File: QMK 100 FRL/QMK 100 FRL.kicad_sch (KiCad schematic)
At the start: 16 parts

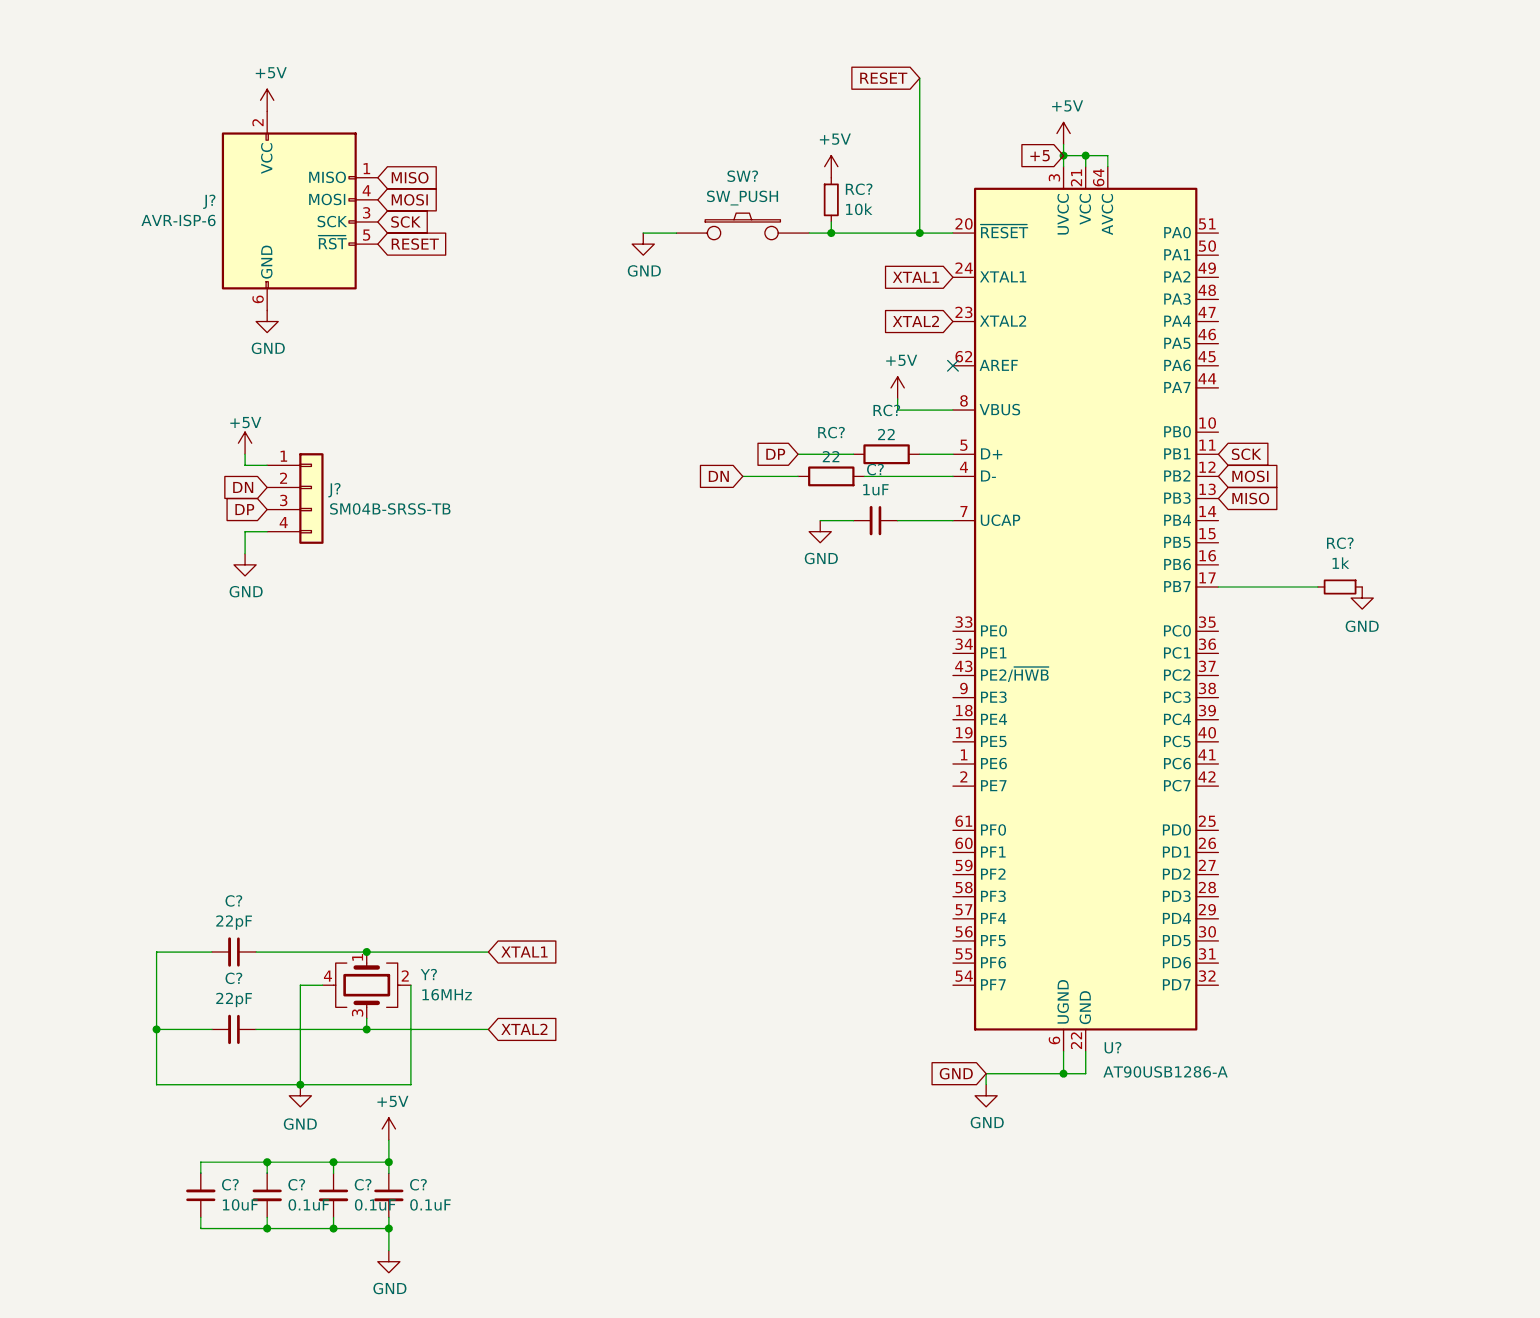
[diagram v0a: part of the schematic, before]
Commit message: Changed MCU
Changed MCU from ATMEL AT90USB1286-AUR to ATMEGA128A-AU which is the newest version.
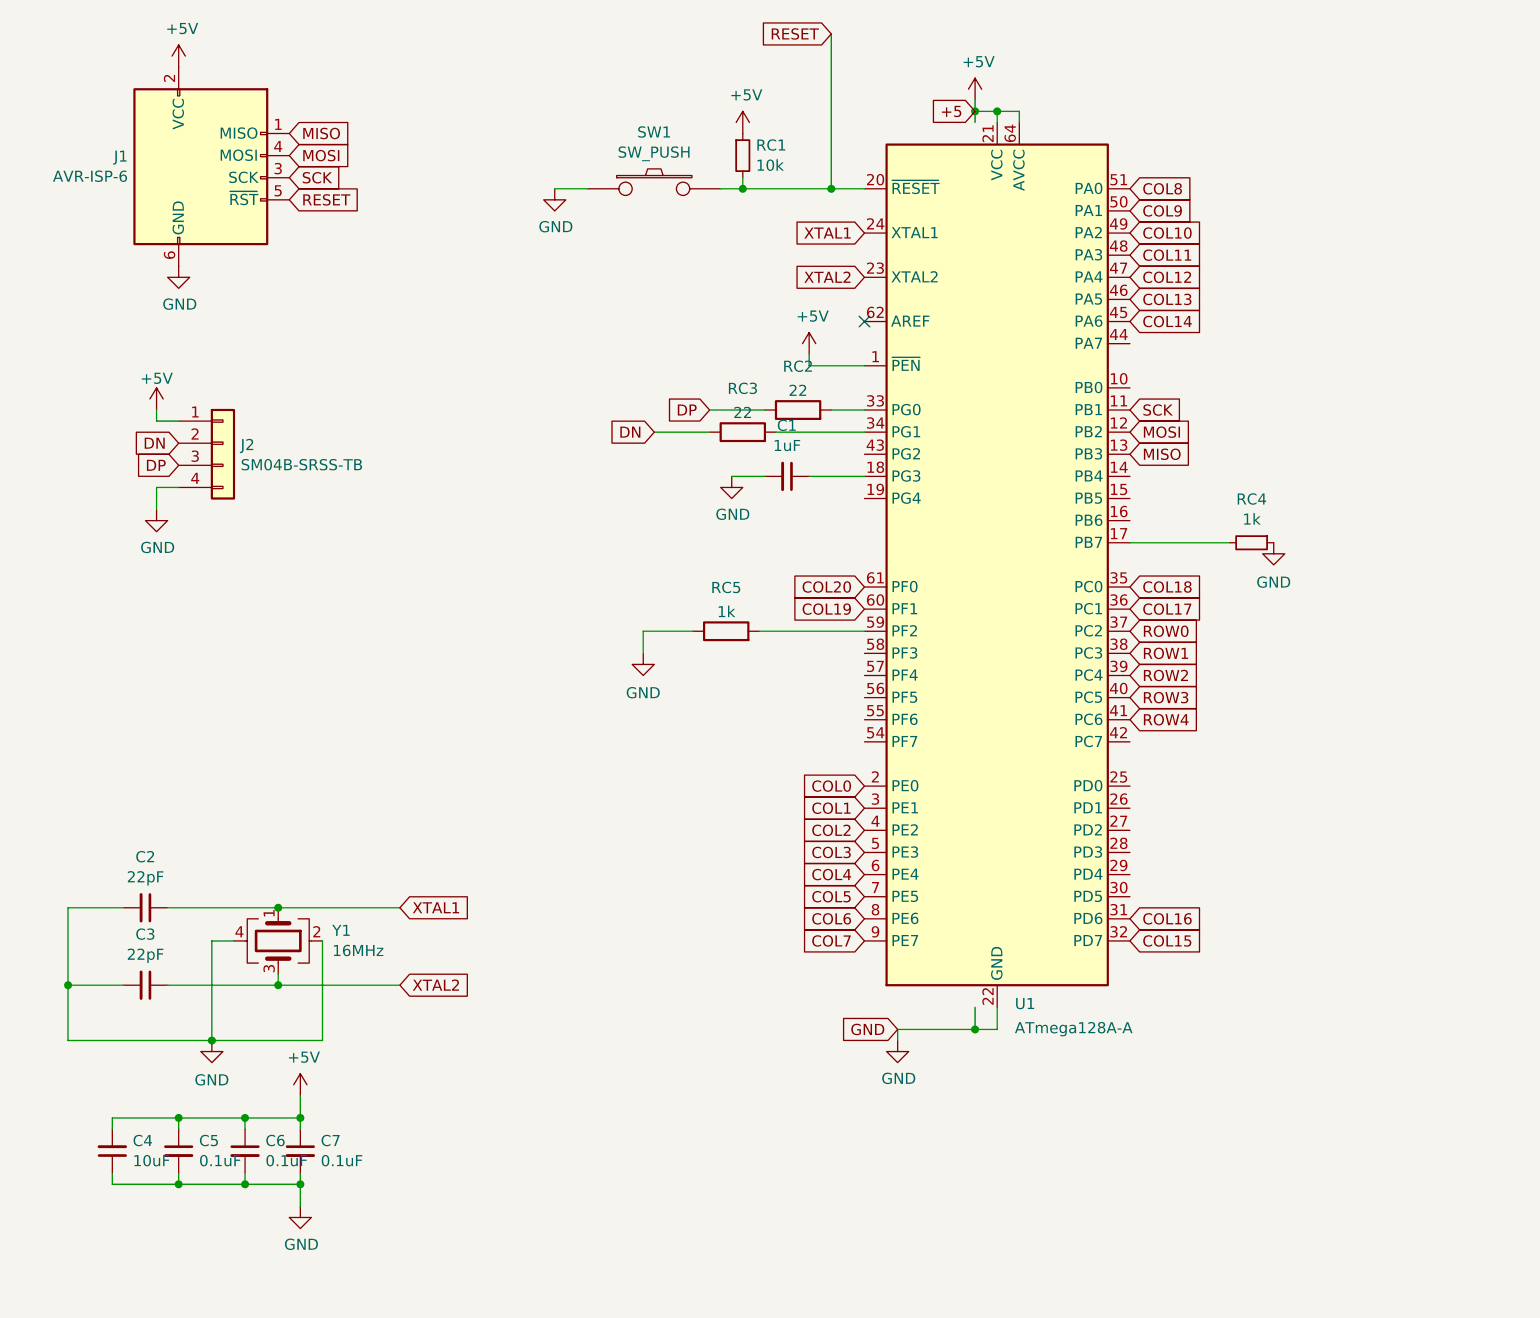
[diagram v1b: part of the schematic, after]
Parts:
- removed U?: AT90USB1286-A, Package_QFP:TQFP-64_14x14mm_P0.8mm, symbol MCU_Microchip_AVR:AT90USB1286-A
- added RC5: 1k, Resistor_SMD:R_0603_1608Metric, symbol Device:R
- added U1: ATmega128A-A, Package_QFP:TQFP-64_14x14mm_P0.8mm, symbol MCU_Microchip_ATmega:ATmega128A-A
- gave numbers to parts that had none: 15
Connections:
- net +5V: now also U1.1 (~{PEN}), U1.21 (VCC), U1.52 (VCC), U1.64 (AVCC)
- net GND: now also RC5.1, U1.22 (GND), U1.53 (GND), U1.63 (GND)
- net MISO: now also U1.13 (PB3)
- net MOSI: now also U1.12 (PB2)
- net RESET: now also U1.20 (~{RESET})
- net SCK: now also U1.11 (PB1)
- net XTAL1: now also U1.24 (XTAL1)
- net XTAL2: now also U1.23 (XTAL2)
- net at RC2.2: now also U1.33 (PG0)
- net at C1.1: now also U1.18 (PG3)
- net at RC4.2: now also U1.17 (PB7)
- net at RC3.2: now also U1.34 (PG1)
- new net: RC5.2, U1.59 (PF2)
- new net COL0: U1.2 (PE0)
- new net COL1: U1.3 (PE1)
- new net COL10: U1.49 (PA2)
- new net COL11: U1.48 (PA3)
- new net COL12: U1.47 (PA4)
- new net COL13: U1.46 (PA5)
- new net COL14: U1.45 (PA6)
- new net COL15: U1.32 (PD7)
- new net COL16: U1.31 (PD6)
- new net COL17: U1.36 (PC1)
- new net COL18: U1.35 (PC0)
- new net COL19: U1.60 (PF1)
- new net COL2: U1.4 (PE2)
- new net COL20: U1.61 (PF0)
- new net COL3: U1.5 (PE3)
- new net COL4: U1.6 (PE4)
- new net COL5: U1.7 (PE5)
- new net COL6: U1.8 (PE6)
- new net COL7: U1.9 (PE7)
- new net COL8: U1.51 (PA0)
- new net COL9: U1.50 (PA1)
- new net ROW0: U1.37 (PC2)
- new net ROW1: U1.38 (PC3)
- new net ROW2: U1.39 (PC4)
- new net ROW3: U1.40 (PC5)
- new net ROW4: U1.41 (PC6)
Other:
- moved on the sheet: C1, C2, C3, C4, C5, C6, C7, J1, J2, RC1, RC2, RC3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

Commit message: working on schematice
adding new items to the pcb using STM32F072CBT6 MCU and resources
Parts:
- removed C1: 1uF, Capacitor_SMD:C_0603_1608Metric, symbol Device:C_Small
- removed C2, C3: 22pF, Capacitor_SMD:C_0603_1608Metric, symbol Device:C_Small
- removed C4: 10uF, Capacitor_SMD:C_0603_1608Metric, symbol Device:C_Small
- removed C5, C6, C7: 0.1uF, Capacitor_SMD:C_0603_1608Metric, symbol Device:C_Small
- removed J1: AVR-ISP-6, random-keyboard-parts:Reset_Pretty-Mask, symbol Connector:AVR-ISP-6
- removed RC1: 10k, Resistor_SMD:R_0603_1608Metric, symbol Device:R_Small
- removed RC2, RC3: 22, Resistor_SMD:R_0603_1608Metric, symbol Device:R
- removed RC4: 1k, Resistor_SMD:R_0603_1608Metric, symbol Device:R_Small
- removed RC5: 1k, Resistor_SMD:R_0603_1608Metric, symbol Device:R
- removed SW1: SW_PUSH, random-keyboard-parts:SKQG-1155865, symbol Keyboard_Parts:SW_PUSH
- removed U1: ATmega128A-A, Package_QFP:TQFP-64_14x14mm_P0.8mm, symbol MCU_Microchip_ATmega:ATmega128A-A
- removed Y1: 16MHz, Crystal:Crystal_SMD_3225-4Pin_3.2x2.5mm, symbol Device:Crystal_GND24
- added C? (x12): C_Small, symbol Device:C_Small
- added D?: D_Schottky, symbol Device:D_Schottky
- added Q?: 2N7002, Package_TO_SOT_SMD:SOT-23, symbol Transistor_FET:2N7002
- added R? (x3): R_Small, symbol Device:R_Small
- added SW?: SW_Push, symbol Switch:SW_Push
- added U?: XC6206PxxxMR, Package_TO_SOT_SMD:SOT-23, symbol Regulator_Linear:XC6206PxxxMR
- added U?: STM32F072CBUx, Package_DFN_QFN:QFN-48-1EP_7x7mm_P0.5mm_EP5.6x5.6mm, symbol MCU_ST_STM32F0:STM32F072CBUx
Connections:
- net +5V: now also C?.1, D?.1 (K)
- net DN: now also U?.32 (PA11)
- net DP: now also U?.33 (PA12)
- net GND: now also C?.1, C?.1, C?.1, C?.1, C?.1, C?.1, C?.1, C?.2, C?.2, Q?.2 (S), R?.2, R?.2, U?.23 (VSS), U?.35 (VSS), U?.47 (VSS), U?.8 (VSSA)
- new net: C?.2, C?.2, U?.1 (GND)
- new net: C?.2, Q?.1 (G), R?.1
- new net +3V3: C?.1, C?.1, C?.2, C?.2, C?.2, C?.2, C?.2, C?.2, C?.2, D?.2 (A), R?.1, SW?.2, U?.1 (VBAT), U?.24 (VDD), U?.36 (VDDIO2), U?.48 (VDD), U?.9 (VDDA)
- new net BOOT0: C?.1, R?.1, SW?.1, U?.44 (BOOT0)
- new net NRST: C?.1, Q?.3 (D), R?.2, U?.7 (NRST)
- new net VSS3: U?.49 (VSS)
- no-connect marks 1 -> 0
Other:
- note added: "VBAT"
- note added: "VDD0 - VSS0"
- note added: "VDD1 - VSS2"
- note added: "VDDA - VSSA"
- note added: "VDDIO2 - VSS1"
- moved on the sheet: J2

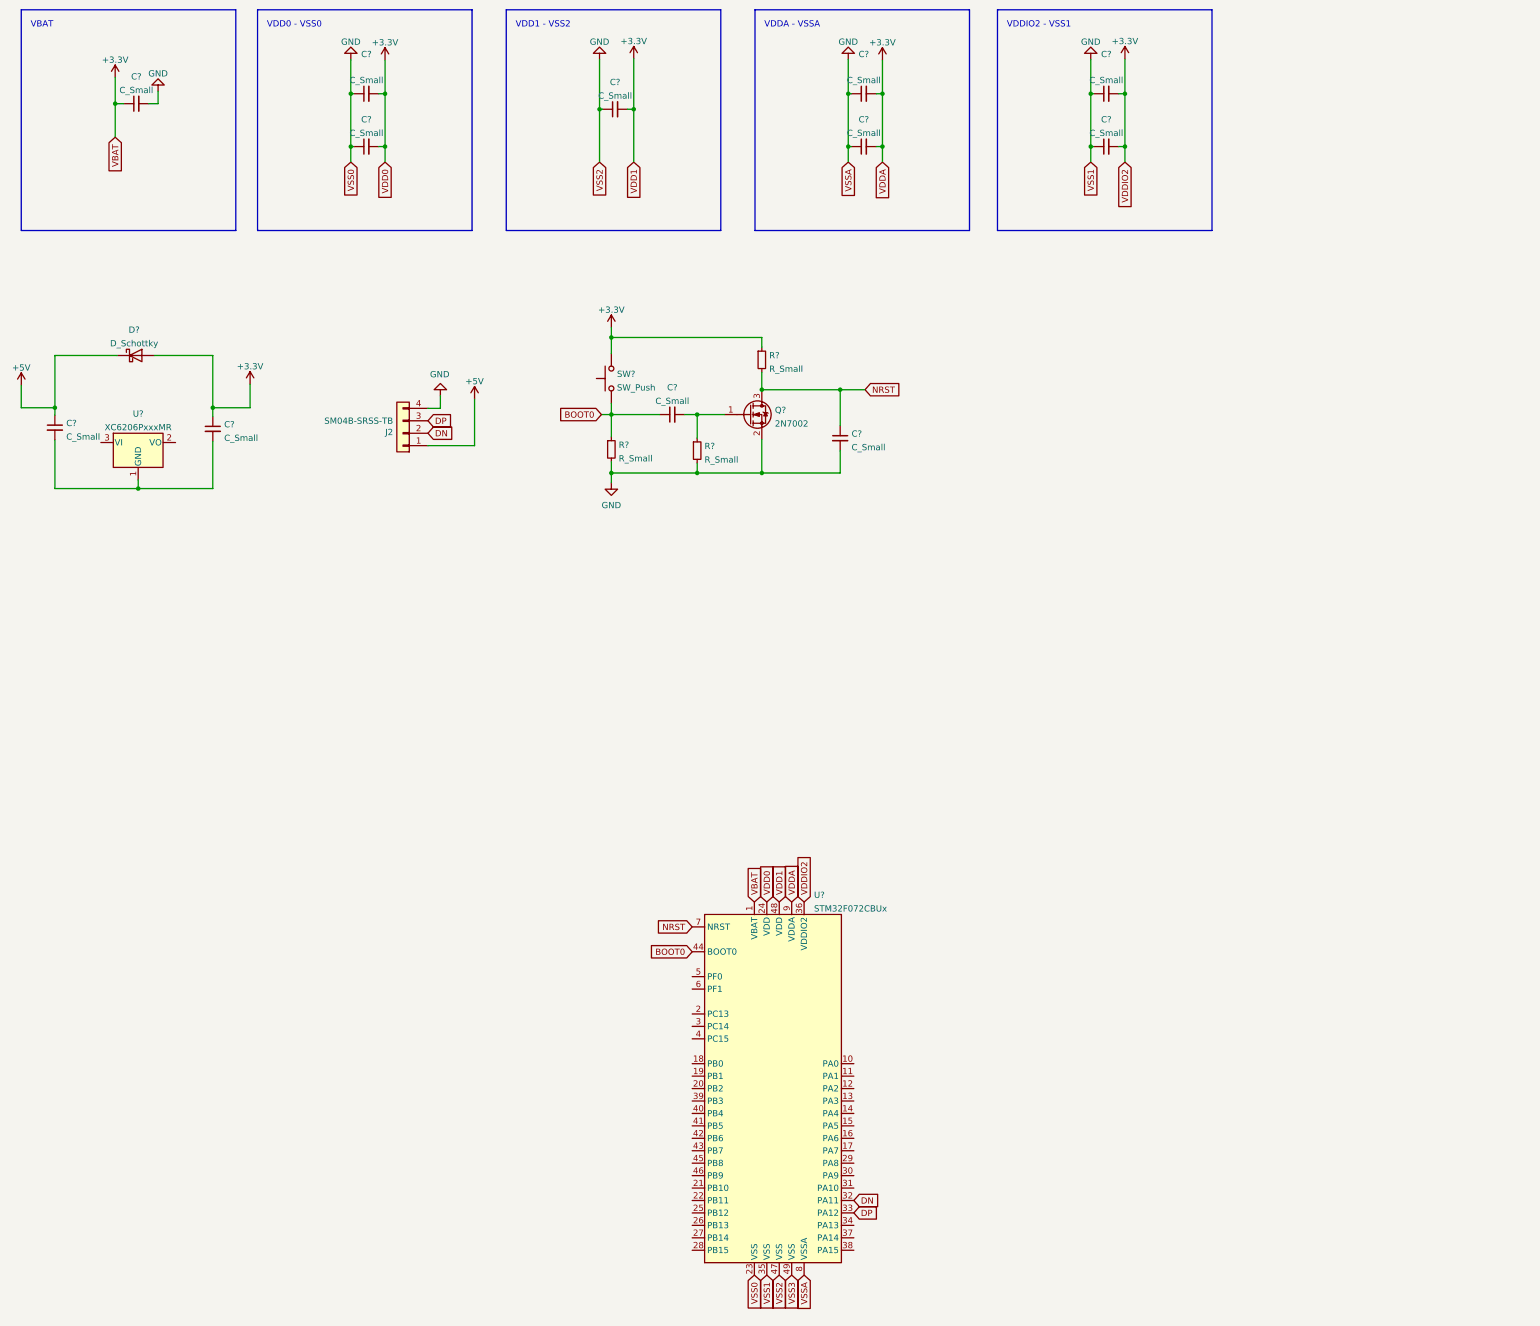
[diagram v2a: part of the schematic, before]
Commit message: Added new acheron library and foot prints
added new files and changed the mcu from STM32F072RBTx to STM32F072R8Tx.
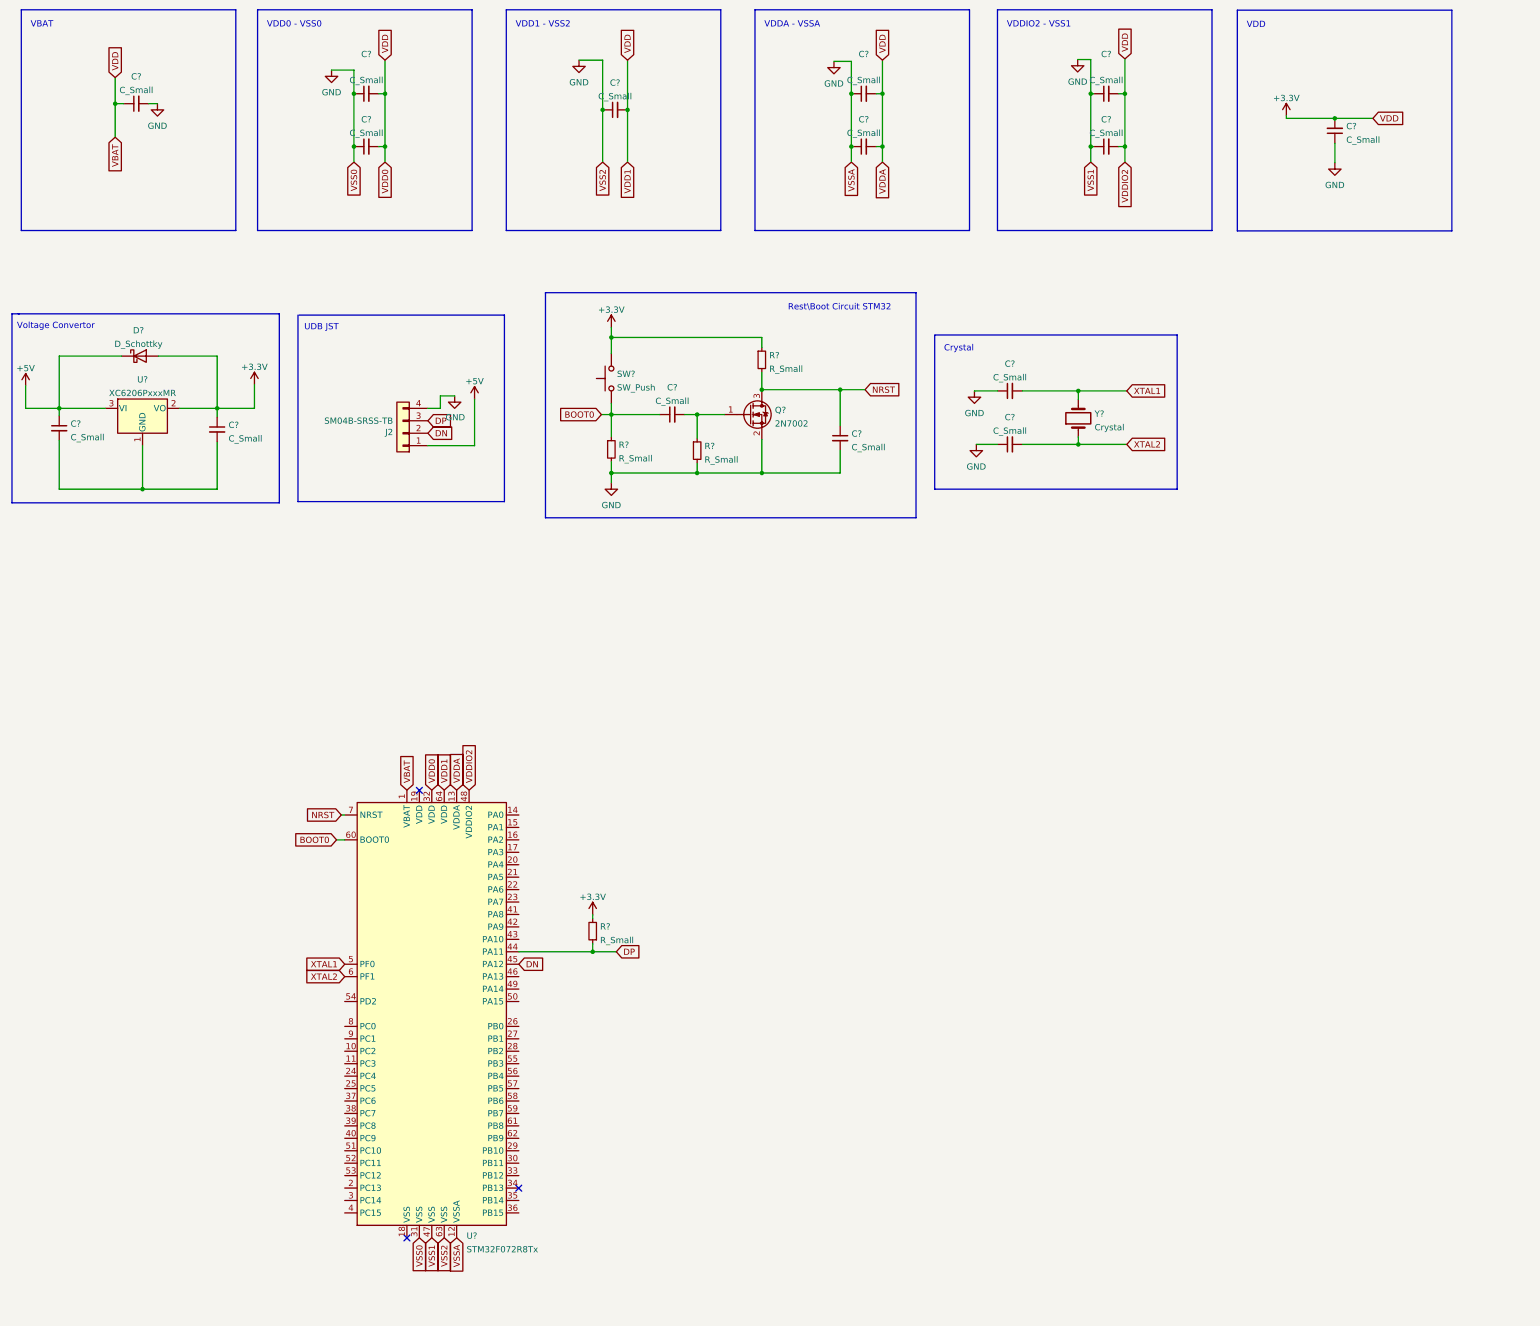
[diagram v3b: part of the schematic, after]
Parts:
- removed U?: STM32F072CBUx, Package_DFN_QFN:QFN-48-1EP_7x7mm_P0.5mm_EP5.6x5.6mm, symbol MCU_ST_STM32F0:STM32F072CBUx
- added C? (x3): C_Small, symbol Device:C_Small
- added R?: R_Small, symbol Device:R_Small
- added U?: STM32F072R8Tx, Package_QFP:LQFP-64_10x10mm_P0.5mm, symbol MCU_ST_STM32F0:STM32F072R8Tx
- added Y?: Crystal, symbol Device:Crystal
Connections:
- net +3V3: now also U?.2 (VO), C?.2, R?.2, U?.1 (VBAT), U?.13 (VDDA), U?.32 (VDD), U?.48 (VDDIO2), U?.64 (VDD)
- net +5V: now also U?.3 (VI)
- net BOOT0: now also U?.60 (BOOT0)
- net DN: now also U?.45 (PA12)
- net GND: now also C?.1, C?.1, C?.1, U?.12 (VSSA), U?.31 (VSS), U?.47 (VSS), U?.63 (VSS)
- net NRST: now also U?.7 (NRST)
- new net: R?.1, U?.44 (PA11)
- new net XTAL1: C?.2, U?.5 (PF0), Y?.2
- new net XTAL2: C?.2, U?.6 (PF1), Y?.1
- no-connect marks 0 -> 3
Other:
- note added: "Crystal"
- note added: "Rest\Boot Circuit STM32"
- note added: "UDB JST"
- note added: "VDD"
- note added: "Voltage Convertor"
- moved on the sheet: C?, D?, U?
